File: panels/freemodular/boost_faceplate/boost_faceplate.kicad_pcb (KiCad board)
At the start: 2 copper layers, 20 x 128.5 mm, 0 parts

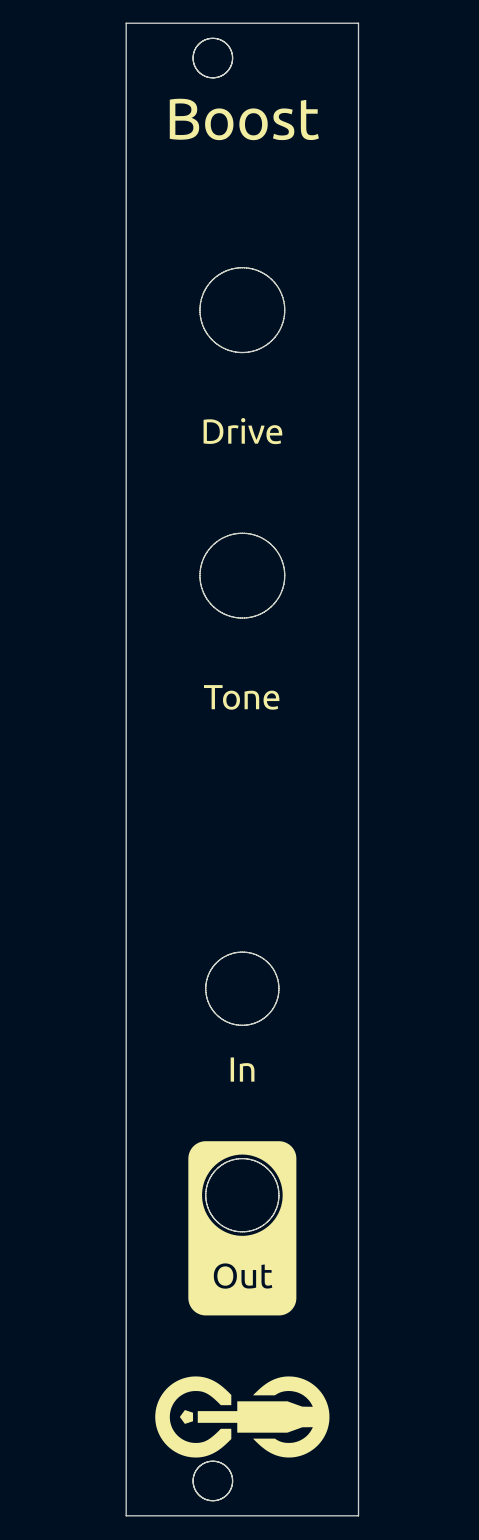
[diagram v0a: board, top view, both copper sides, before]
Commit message: mod2 firmwares, new faceplates
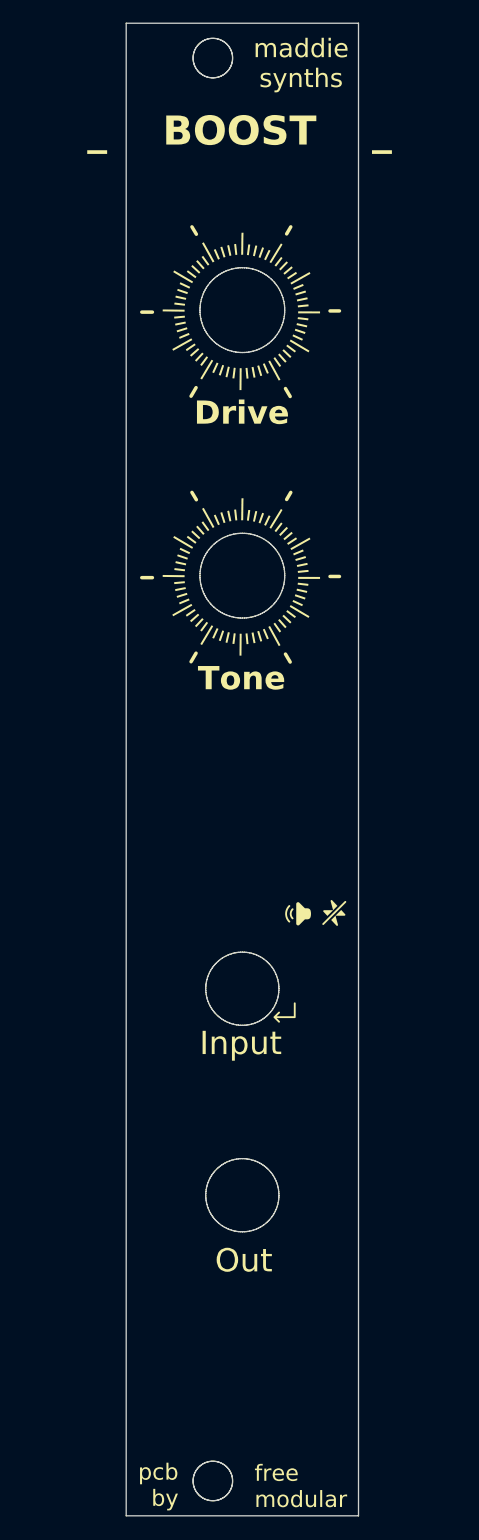
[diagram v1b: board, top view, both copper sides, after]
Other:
- board text added: "Drive"
- board text added: "Input"
- board text added: "Out"
- board text added: "Tone"
- board text added: "_ BOOST _"
- board text added: "free modular"
- board text added: "maddie synths"
- board text added: "pcb by"
